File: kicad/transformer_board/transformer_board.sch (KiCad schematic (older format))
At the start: 35 parts, among them J1 Conn_01x01, J2 Conn_01x01, J3 Conn_01x01, J4 Conn_01x01, J5 Conn_01x01, J6 Conn_01x01, J7 Conn_01x01, J8 Conn_01x01, J9 Conn_01x01, T1 14A-30-515, U1 LM317_TO-220, U2 LM337_TO220

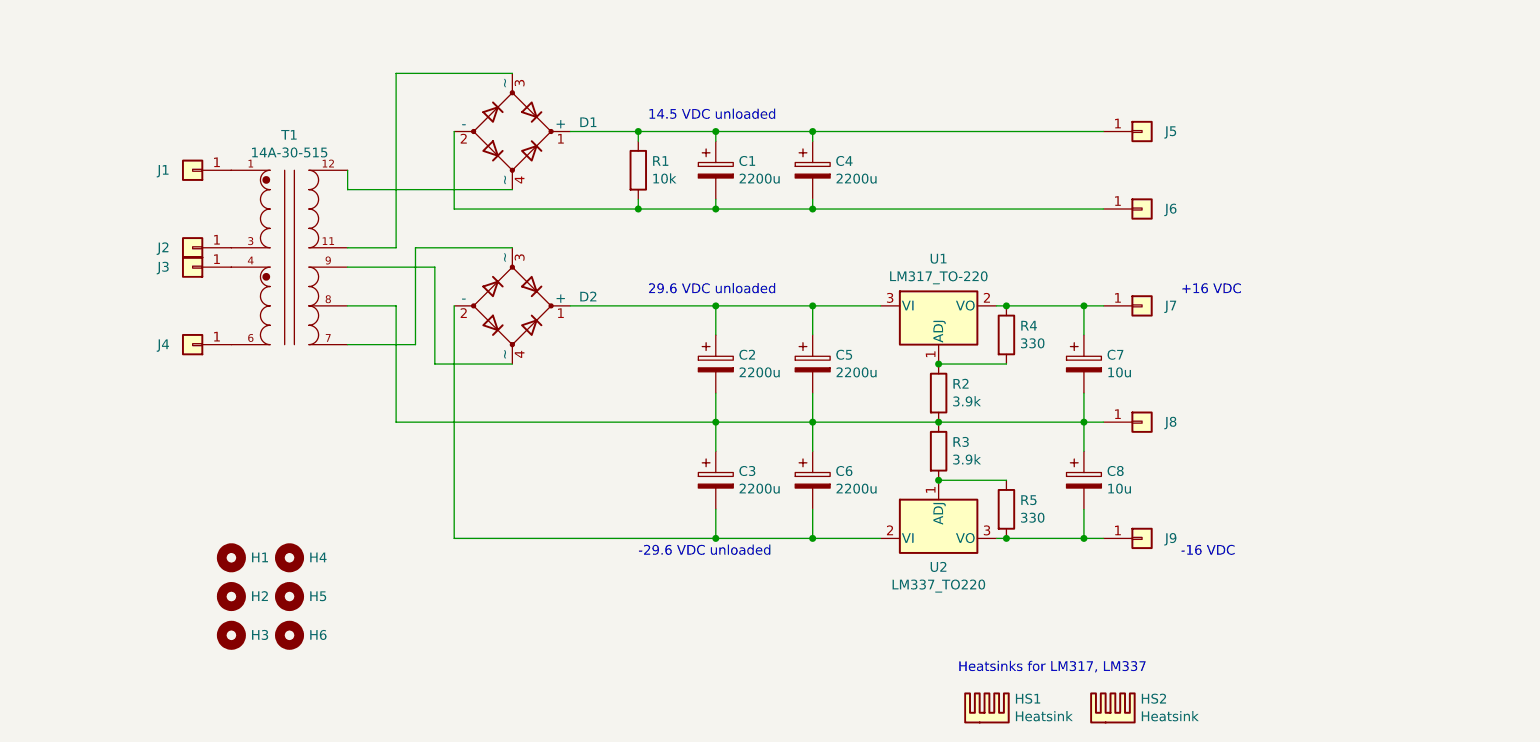
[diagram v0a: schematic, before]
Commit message: Added preregs to all rails.
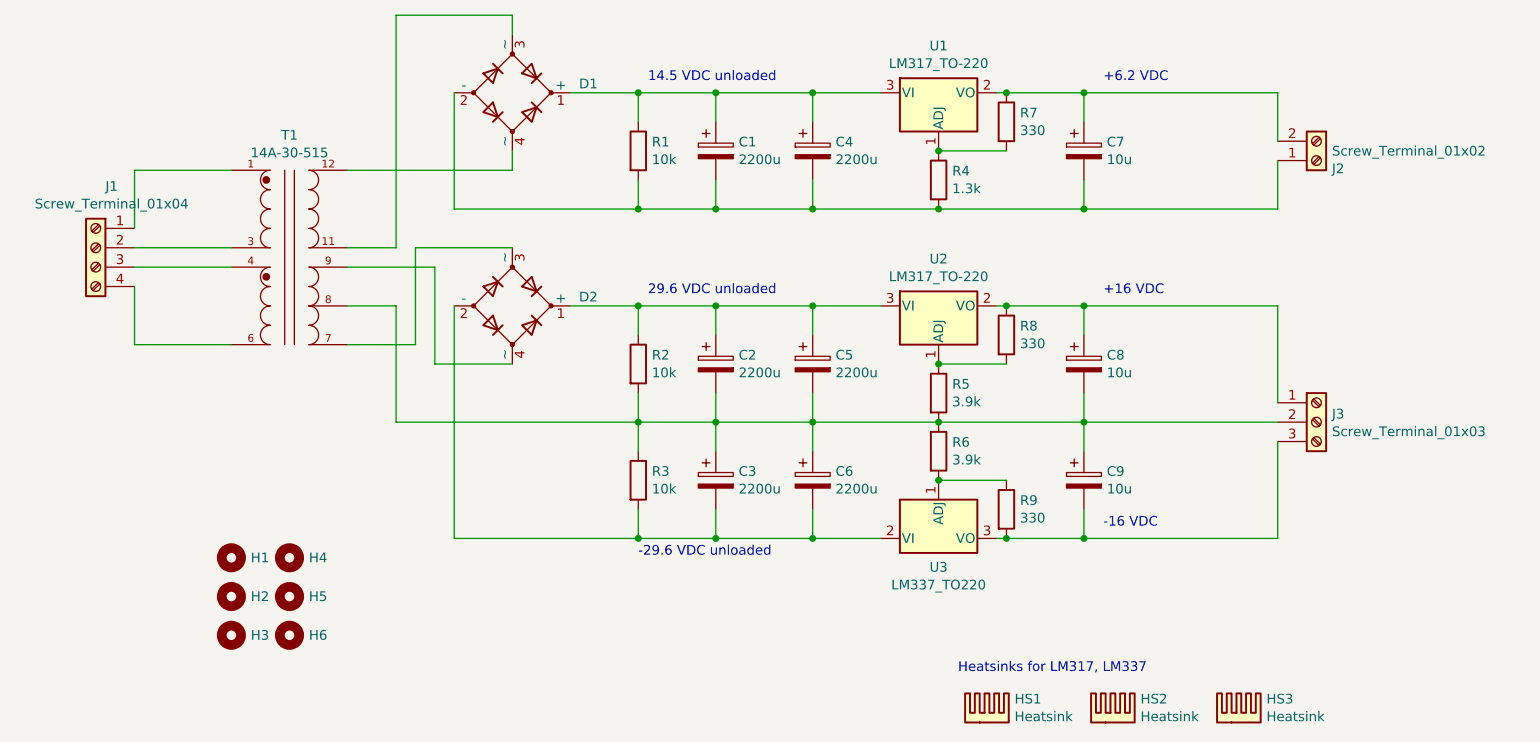
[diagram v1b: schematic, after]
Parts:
- removed J1, J2, J3, J4, J5, J6, J7, J8, J9: Conn_01x01, Connector_Wire:SolderWirePad_1x01_Drill1.5mm, symbol Connector_Generic:Conn_01x01
- added C9: 10u, Capacitor_THT:CP_Radial_D5.0mm_P2.00mm, symbol Device:CP
- added HS3: Heatsink, project_footprints:AAVID_504102B00000G, symbol Mechanical:Heatsink
- added J1: Screw_Terminal_01x04, TerminalBlock_Phoenix:TerminalBlock_Phoenix_PT-1,5-4-5.0-H_1x04_P5.00mm_Horizontal, symbol Connector:Screw_Terminal_01x04
- added J2: Screw_Terminal_01x02, TerminalBlock_Phoenix:TerminalBlock_Phoenix_PT-1,5-2-5.0-H_1x02_P5.00mm_Horizontal, symbol Connector:Screw_Terminal_01x02
- added J3: Screw_Terminal_01x03, TerminalBlock_Phoenix:TerminalBlock_Phoenix_PT-1,5-3-5.0-H_1x03_P5.00mm_Horizontal, symbol Connector:Screw_Terminal_01x03
- added R2, R3: 10k, Resistor_THT:R_Axial_DIN0207_L6.3mm_D2.5mm_P7.62mm_Horizontal, symbol Device:R
- added R4: 1.3k, Resistor_THT:R_Axial_DIN0207_L6.3mm_D2.5mm_P7.62mm_Horizontal, symbol Device:R
- added R7: 330, Resistor_THT:R_Axial_DIN0207_L6.3mm_D2.5mm_P7.62mm_Horizontal, symbol Device:R
- added U1: LM317_TO-220, Package_TO_SOT_THT:TO-220-3_Horizontal_TabDown, symbol Regulator_Linear:LM317_TO-220
- C7, C8: DigiKey 565-4993-1-ND -> 732-9501-1-ND
- R5: renamed from R2; DigiKey 56-SFR25H0003901FR500CT-ND -> 56-SFR2500003901FR500CT-ND
- R6: renamed from R3; DigiKey 56-SFR25H0003901FR500CT-ND -> 56-SFR2500003901FR500CT-ND
- R9: renamed from R5; DigiKey 56-SFR25H0003300FR500CT-ND -> BC4366CT-ND
- renumbered R4 to R8, U1 to U2, U2 to U3
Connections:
- net at T1.1: now also J1.1 (Pin_1)
- net at T1.3: now also J1.2 (Pin_2)
- net at T1.4: now also J1.3 (Pin_3)
- net at T1.6: now also J1.4 (Pin_4)
- net at C2.2, C3.1, C5.2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: now also C8.2, C9.1, J3.2 (Pin_2), R2.2, R3.1; no longer C7.2, C8.1
- net at C1.1, C4.1, D1.1 (+)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: now also U1.3 (VI)
- net at C1.2, C4.2, D1.2 (-)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: now also C7.2, J2.1 (Pin_1), R4.2
- net at C2.1, C5.1, D2.1 (+)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: now also R2.1
- net at C3.2, C6.2, D2.2 (-)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: now also R3.2
- net at R8.1, U2.2 (VO): now also C8.1, J3.1 (Pin_1); no longer C7.1
- net at R9.2, U3.3 (VO): now also C9.2, J3.3 (Pin_3); no longer C8.2
- new net: R4.1, R7.2, U1.1 (ADJ)
- new net: C7.1, J2.2 (Pin_2), R7.1, U1.2 (VO)
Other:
- note added: "+6.2 VDC"
- moved on the sheet: C1, C4, D1, R1

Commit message: Fixed error in silkscreen
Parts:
- J2: DigiKey (none) -> 277-1667-ND
- J3: DigiKey (none) -> 277-1578-ND
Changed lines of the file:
@@
 F 2 "TerminalBlock_Phoenix:TerminalBlock_Phoenix_PT-1,5-3-5.0-H_1x03_P5.00mm_Horizontal" H 9600 4300 50  0001 C CNN
 F 3 "~" H 9600 4300 50  0001 C CNN
-F 4 "" H 9600 4300 50  0001 C CNN "DigiKey"
+F 4 "277-1578-ND" H 9600 4300 50  0001 C CNN "DigiKey"
 	1    9600 4300
 	1    0    0    -1
@@
 F 2 "TerminalBlock_Phoenix:TerminalBlock_Phoenix_PT-1,5-2-5.0-H_1x02_P5.00mm_Horizontal" H 9600 2950 50  0001 C CNN
 F 3 "~" H 9600 2950 50  0001 C CNN
-F 4 "" H 9600 2950 50  0001 C CNN "DigiKey"
+F 4 "277-1667-ND" H 9600 2950 50  0001 C CNN "DigiKey"
 	1    9600 2950
 	1    0    0    1
